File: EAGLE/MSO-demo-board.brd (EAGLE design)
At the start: 68.2 x 55.9 mm, 43 parts, among them IC1 ATMEGA168-20P, J1 AVR_SPI_PRG_62X3_LOCK

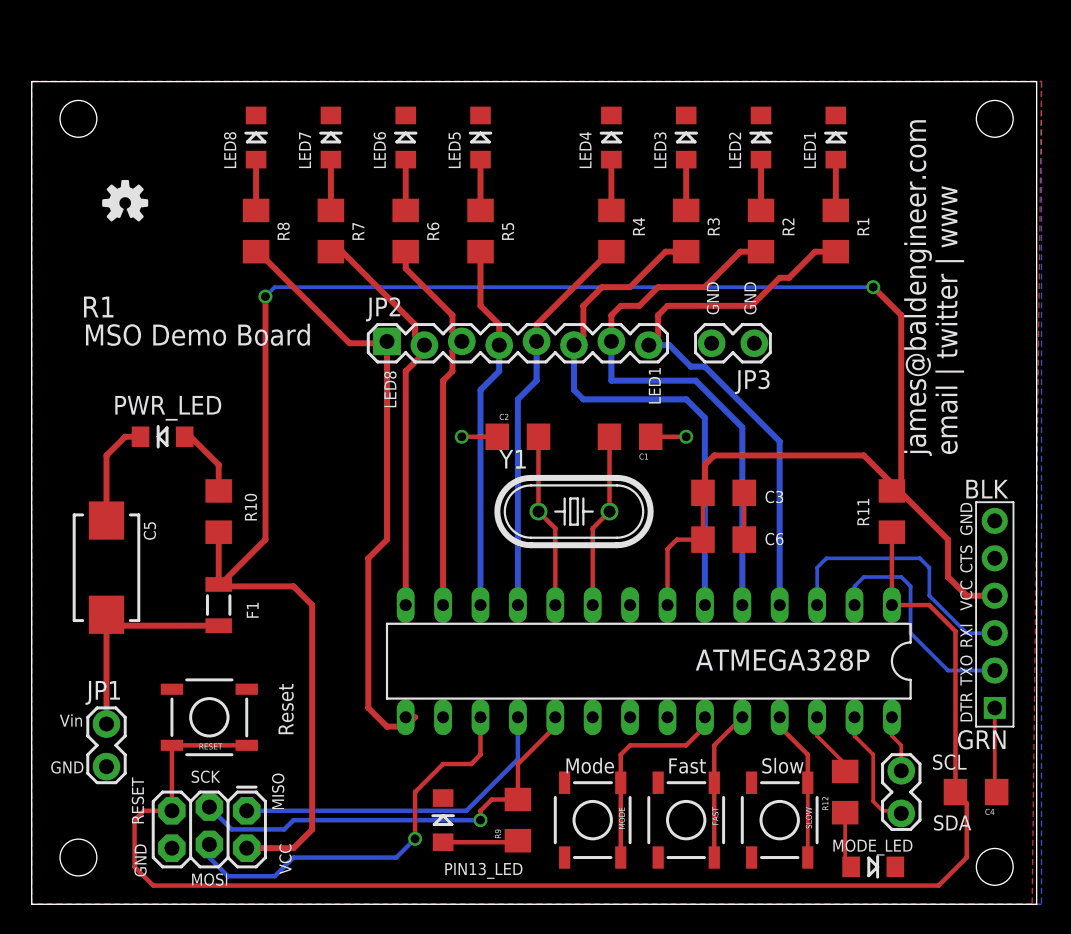
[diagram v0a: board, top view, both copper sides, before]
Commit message: Fixed VCC Grounded mistake
AVCC was tied to ground causing a short at power up.  Tied AVCC and
AREF to 5V instead of ground.  Also swapped TX and RX on FTDI pinout
(was backwards)
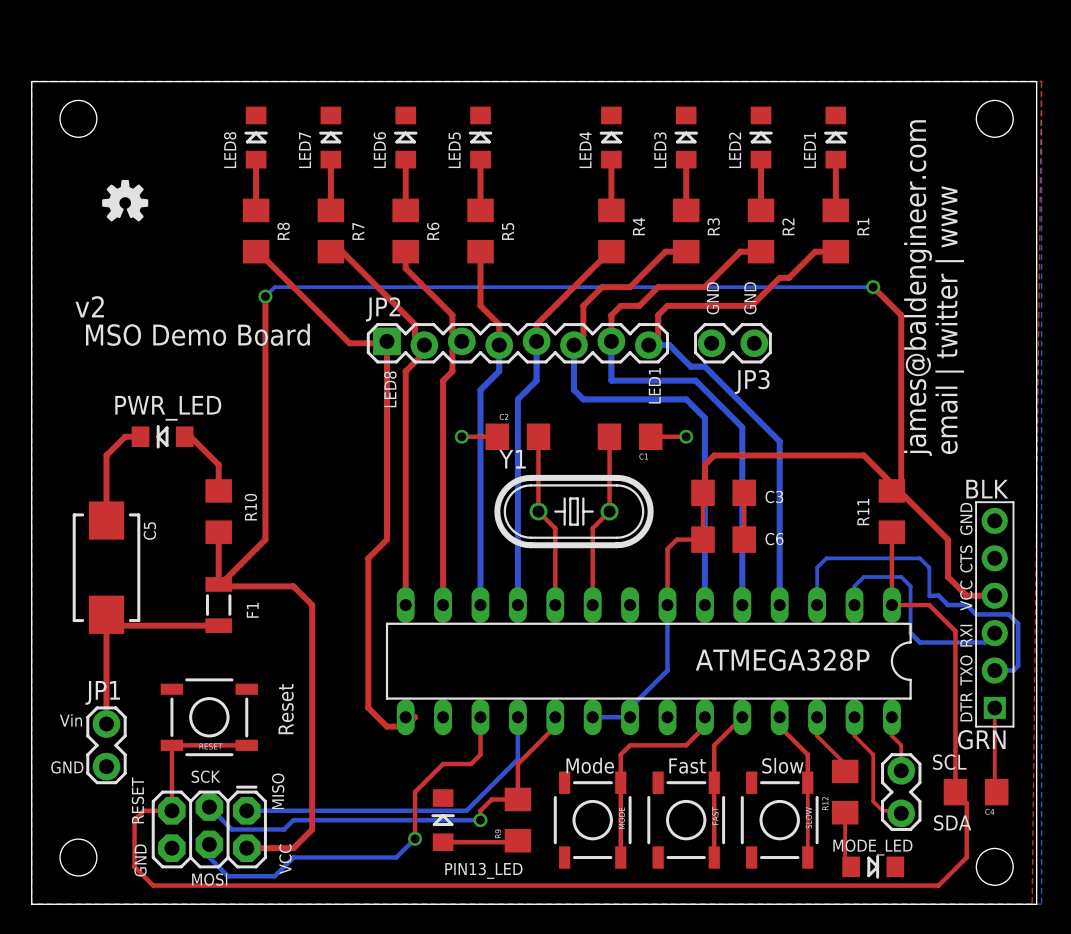
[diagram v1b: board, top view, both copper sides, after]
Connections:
- net GND: no longer IC1.20, IC1.21
- net RXD: now also JP4.P$3; no longer JP4.P$2
- net TXD: now also JP4.P$2; no longer JP4.P$3
- net VCC: now also IC1.20, IC1.21
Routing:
- net VCC: track 145.8 -> 157.0 mm
- net TXD: track 18.1 -> 24.0 mm
- net RXD: track 15.5 -> 15.0 mm
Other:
- board text added: "v2"
- board text removed: "R1"
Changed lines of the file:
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@@
 <setting verticaltext="up"/>
 </settings>
-<grid distance="25" unitdist="mil" unit="inch" style="lines" multiple="1" display="no" altdistance="12.5" altunitdist="mil" altunit="mil"/>
+<grid distance="25" unitdist="mil" unit="mil" style="lines" multiple="1" display="no" altdistance="12.5" altunitdist="mil" altunit="mil"/>
 <layers>
 <layer number="1" name="Top" color="4" fill="1" visible="yes" active="yes"/>
@@
 email | twitter | www</text>
 <text x="19.05" y="39.37" size="1.4224" layer="25" rot="R180">MSO Demo Board</text>
-<text x="5.715" y="41.275" size="1.4224" layer="25" rot="R180">R1</text>
+<text x="5.08" y="41.275" size="1.4224" layer="25" rot="R180">v2</text>
 </plain>
 <attributes>
@@
 </elements>
 <signals>
-<signal name="GND">
+<signal name="GND" airwireshidden="yes">
 <contactref element="RESET" pad="3"/>
 <contactref element="RESET" pad="4"/>
@@
 <contactref element="LED8" pad="C"/>
 <contactref element="IC1" pad="22"/>
-<contactref element="IC1" pad="21"/>
-<contactref element="IC1" pad="20"/>
 <contactref element="IC1" pad="8"/>
 <contactref element="C6" pad="1"/>
@@
 <wire x1="57.15" y1="41.91" x2="16.51" y2="41.91" width="0.254" layer="16"/>
 <wire x1="16.51" y1="41.91" x2="15.875" y2="41.275" width="0.254" layer="16"/>
+<contactref element="IC1" pad="21"/>
+<contactref element="IC1" pad="20"/>
+<wire x1="38.1" y1="12.7" x2="40.64" y2="12.7" width="0.3048" layer="16"/>
+<wire x1="40.64" y1="12.7" x2="40.64" y2="13.335" width="0.3048" layer="16"/>
+<wire x1="40.64" y1="13.335" x2="43.18" y2="15.875" width="0.3048" layer="16"/>
+<wire x1="43.18" y1="15.875" x2="43.18" y2="20.32" width="0.3048" layer="16"/>
 </signal>
 <signal name="RESET">
@@
 <signal name="RXD">
 <contactref element="IC1" pad="2"/>
-<contactref element="JP4" pad="P$2"/>
 <wire x1="55.88" y1="20.32" x2="55.88" y2="21.59" width="0.254" layer="16"/>
 <wire x1="55.88" y1="21.59" x2="56.515" y2="22.225" width="0.254" layer="16"/>
@@
 <wire x1="59.055" y1="22.225" x2="59.69" y2="21.59" width="0.254" layer="16"/>
 <wire x1="59.69" y1="21.59" x2="59.69" y2="18.415" width="0.254" layer="16"/>
-<wire x1="59.69" y1="18.415" x2="62.23" y2="15.875" width="0.254" layer="16"/>
-<wire x1="62.23" y1="15.875" x2="65.405" y2="15.875" width="0.254" layer="16"/>
+<contactref element="JP4" pad="P$3"/>
+<wire x1="59.69" y1="18.415" x2="60.325" y2="17.78" width="0.3048" layer="16"/>
+<wire x1="60.325" y1="17.78" x2="64.77" y2="17.78" width="0.3048" layer="16"/>
+<wire x1="64.77" y1="17.78" x2="65.405" y2="18.415" width="0.3048" layer="16"/>
 </signal>
 <signal name="TXD">
 <contactref element="IC1" pad="3"/>
-<contactref element="JP4" pad="P$3"/>
 <wire x1="53.34" y1="20.32" x2="53.34" y2="22.86" width="0.254" layer="16"/>
 <wire x1="53.34" y1="22.86" x2="53.975" y2="23.495" width="0.254" layer="16"/>
@@
 <wire x1="60.325" y1="23.495" x2="60.96" y2="22.86" width="0.254" layer="16"/>
 <wire x1="60.96" y1="22.86" x2="60.96" y2="20.955" width="0.254" layer="16"/>
-<wire x1="60.96" y1="20.955" x2="63.5" y2="18.415" width="0.254" layer="16"/>
-<wire x1="63.5" y1="18.415" x2="65.405" y2="18.415" width="0.254" layer="16"/>
+<contactref element="JP4" pad="P$2"/>
+<wire x1="60.96" y1="20.955" x2="61.595" y2="20.955" width="0.3048" layer="16"/>
+<wire x1="61.595" y1="20.955" x2="62.23" y2="20.32" width="0.3048" layer="16"/>
+<wire x1="62.23" y1="20.32" x2="63.5" y2="20.32" width="0.3048" layer="16"/>
+<wire x1="63.5" y1="20.32" x2="64.135" y2="19.685" width="0.3048" layer="16"/>
+<wire x1="64.135" y1="19.685" x2="66.3575" y2="19.685" width="0.3048" layer="16"/>
+<wire x1="66.3575" y1="19.685" x2="66.9925" y2="19.05" width="0.3048" layer="16"/>
+<wire x1="66.9925" y1="19.05" x2="66.9925" y2="16.1925" width="0.3048" layer="16"/>
+<wire x1="66.9925" y1="16.1925" x2="66.675" y2="15.875" width="0.3048" layer="16"/>
+<wire x1="66.675" y1="15.875" x2="65.405" y2="15.875" width="0.3048" layer="16"/>
 </signal>
 <signal name="SDA">
